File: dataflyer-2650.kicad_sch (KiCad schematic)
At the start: 2 parts, among them J1 26-pin IDC (Dataflyer side), J2 50-pin IDC (SCSI chain out)

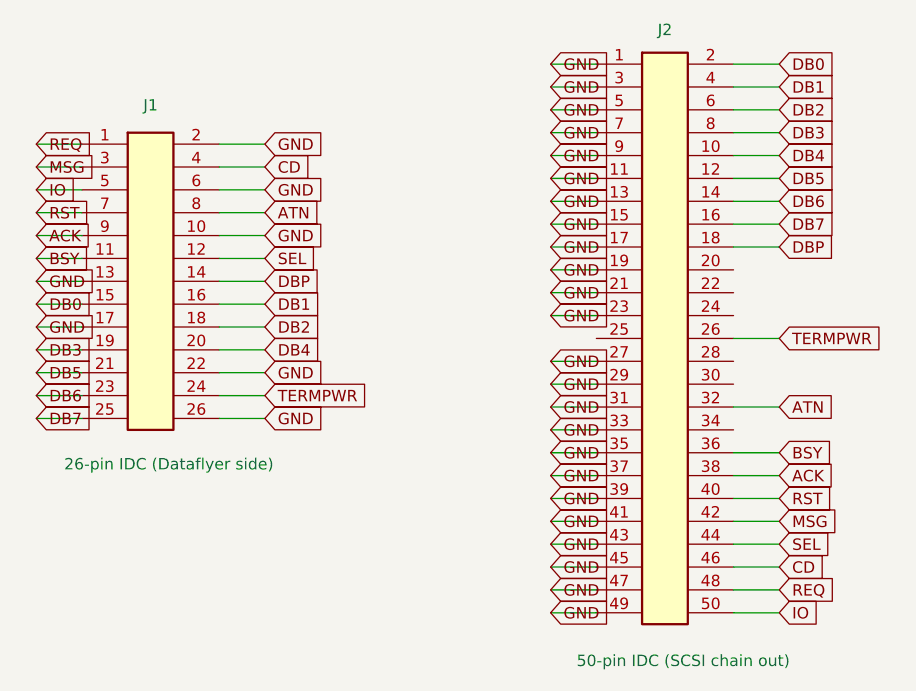
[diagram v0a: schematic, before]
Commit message: Release 1.1: GND reserved IDC50 pins; J1 moved inboard
Schematic: connect SCSI-1 reserved IDC50 pins 20, 22, 24, 28, 30, 34
to GND for cleaner signaling and to match common SCSI-1 controller
practice (these were left floating in 1.0).

PCB: J1 shifted ~3.5 mm inboard for easier routing. Board outline
(73.5 x 35 mm) and connector mating are unchanged — does not affect
fit with DataFlyer 1200 SCSI+ or Phase5 Blizzard IV SCSI kit.

Docs: README revision history, PINOUT.md IDC50 ground net section.
KiCad schematic rev bumped 1.0 -> 1.1 (PCB internal rev left at 1.8).
Freerouting artifacts (.dsn/.ses/.rules) re-exported.

(c) 2026 Arnljot Arntsen
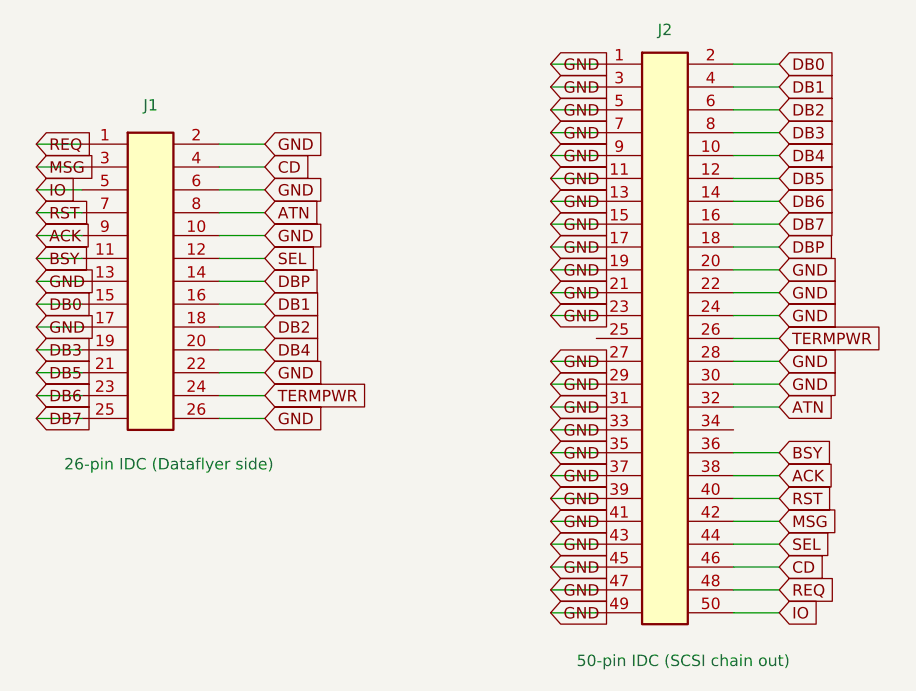
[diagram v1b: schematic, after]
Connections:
- net GND: now also J2.20 (Pin_20), J2.22 (Pin_22), J2.24 (Pin_24), J2.28 (Pin_28), J2.30 (Pin_30)
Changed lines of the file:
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@@
 		(title "Dataflyer 1200 SCSI+ 26pin to 50pin Adapter")
 		(date "2026-06-02")
-		(rev "1.0")
+		(rev "1.1")
 		(comment 1 "For Dataflyer 1200 SCSI+ And Phase5 Blizzard IV SCSI kit")
 		(comment 2 "Based on SCSI cable by highpuff iKod.se")
@@
 	(wire
 		(pts
+			(xy 162.56 60.96) (xy 167.64 60.96)
+		)
+		(stroke
+			(width 0)
+			(type default)
+		)
+	)
+	(wire
+		(pts
 			(xy 162.56 81.28) (xy 167.64 81.28)
 		)
@@
 	(wire
 		(pts
+			(xy 162.56 55.88) (xy 167.64 55.88)
+		)
+		(stroke
+			(width 0)
+			(type default)
+		)
+	)
+	(wire
+		(pts
 			(xy 162.56 33.02) (xy 167.64 33.02)
 		)
@@
 	(wire
 		(pts
+			(xy 162.56 63.5) (xy 167.64 63.5)
+		)
+		(stroke
+			(width 0)
+			(type default)
+		)
+	)
+	(wire
+		(pts
+			(xy 162.56 53.34) (xy 167.64 53.34)
+		)
+		(stroke
+			(width 0)
+			(type default)
+		)
+	)
+	(wire
+		(pts
 			(xy 105.41 49.53) (xy 110.49 49.53)
 		)
@@
 	(wire
 		(pts
+			(xy 162.56 50.8) (xy 167.64 50.8)
+		)
+		(stroke
+			(width 0)
+			(type default)
+		)
+	)
+	(wire
+		(pts
 			(xy 105.41 41.91) (xy 110.49 41.91)
 		)
@@
 		)
 	)
+	(global_label "GND"
+		(shape input)
+		(at 167.64 60.96 0)
+		(fields_autoplaced yes)
+		(effects
+			(font
+				(size 1.27 1.27)
+			)
+			(justify left)
+		)
+		(property "Intersheetrefs" "${INTERSHEET_REFS}"
+			(at 167.64 60.96 0)
+			(hide yes)
+			(show_name no)
+			(do_not_autoplace no)
+			(effects
+				(font
+					(size 1.27 1.27)
+				)
+			)
+		)
+	)
 	(global_label "IO"
 		(shape input)
@@
 		)
 	)
+	(global_label "GND"
+		(shape input)
+		(at 167.64 55.88 0)
+		(fields_autoplaced yes)
+		(effects
+			(font
+				(size 1.27 1.27)
+			)
+			(justify left)
+		)
+		(property "Intersheetrefs" "${INTERSHEET_REFS}"
+			(at 167.64 55.88 0)
+			(hide yes)
+			(show_name no)
+			(do_not_autoplace no)
+			(effects
+				(font
+					(size 1.27 1.27)
+				)
+			)
+		)
+	)
 	(global_label "DB1"
 		(shape input)
@@
 		)
 	)
+	(global_label "GND"
+		(shape input)
+		(at 167.64 63.5 0)
+		(fields_autoplaced yes)
+		(effects
+			(font
+				(size 1.27 1.27)
+			)
+			(justify left)
+		)
+		(property "Intersheetrefs" "${INTERSHEET_REFS}"
+			(at 167.64 63.5 0)
+			(hide yes)
+			(show_name no)
+			(do_not_autoplace no)
+			(effects
+				(font
+					(size 1.27 1.27)
+				)
+			)
+		)
+	)
 	(global_label "DB7"
 		(shape input)
@@
 		)
 	)
+	(global_label "GND"
+		(shape input)
+		(at 167.64 53.34 0)
+		(fields_autoplaced yes)
+		(effects
+			(font
+				(size 1.27 1.27)
+			)
+			(justify left)
+		)
+		(property "Intersheetrefs" "${INTERSHEET_REFS}"
+			(at 167.64 53.34 0)
+			(hide yes)
+			(show_name no)
+			(do_not_autoplace no)
+			(effects
+				(font
+					(size 1.27 1.27)
+				)
+			)
+		)
+	)
 	(global_label "MSG"
 		(shape input)
@@
 			(hide yes)
 			(show_name no)
+			(do_not_autoplace no)
+			(effects
+				(font
+					(size 1.27 1.27)
+				)
+			)
+		)
+	)
+	(global_label "GND"
+		(shape input)
+		(at 167.64 50.8 0)
+		(fields_autoplaced yes)
+		(effects
+			(font
+				(size 1.27 1.27)
+			)
+			(justify left)
+		)
+		(property "Intersheetrefs" "${INTERSHEET_REFS}"
+			(at 167.64 50.8 0)
+			(hide yes)
+			(show_name no)

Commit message: Docs/KiCad: sync schematic title, PCB rev, and PINOUT references
- Schematic title: "Dataflyer 1200 SCSI+ 26pin to 50pin Adapter"
  -> "DataFlyer 2650 — 26-pin to 50-pin SCSI Adapter"
- PCB rev: 1.8 -> 1.1 (sync with schematic and README revision history)
- PINOUT.md: add cdmediaworld.com 50-pin SCSI-1 pinout reference

(c) 2026 Arnljot Arntsen
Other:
- title: Dataflyer 1200 SCSI+ 26pin to 50pin Adapter -> DataFlyer 2650 — 26-pin to 50-pin SCSI Adapter
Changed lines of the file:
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@@
 	(paper "A5")
 	(title_block
-		(title "Dataflyer 1200 SCSI+ 26pin to 50pin Adapter")
+		(title "DataFlyer 2650 — 26-pin to 50-pin SCSI Adapter")
 		(date "2026-06-02")
 		(rev "1.1")
